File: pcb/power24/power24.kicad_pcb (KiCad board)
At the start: 2 copper layers, 47.8 x 64 mm, 24 parts, among them P1 CONN_3X2, P2 CONN_4X2, P3 CONN_2, U1 MC34063

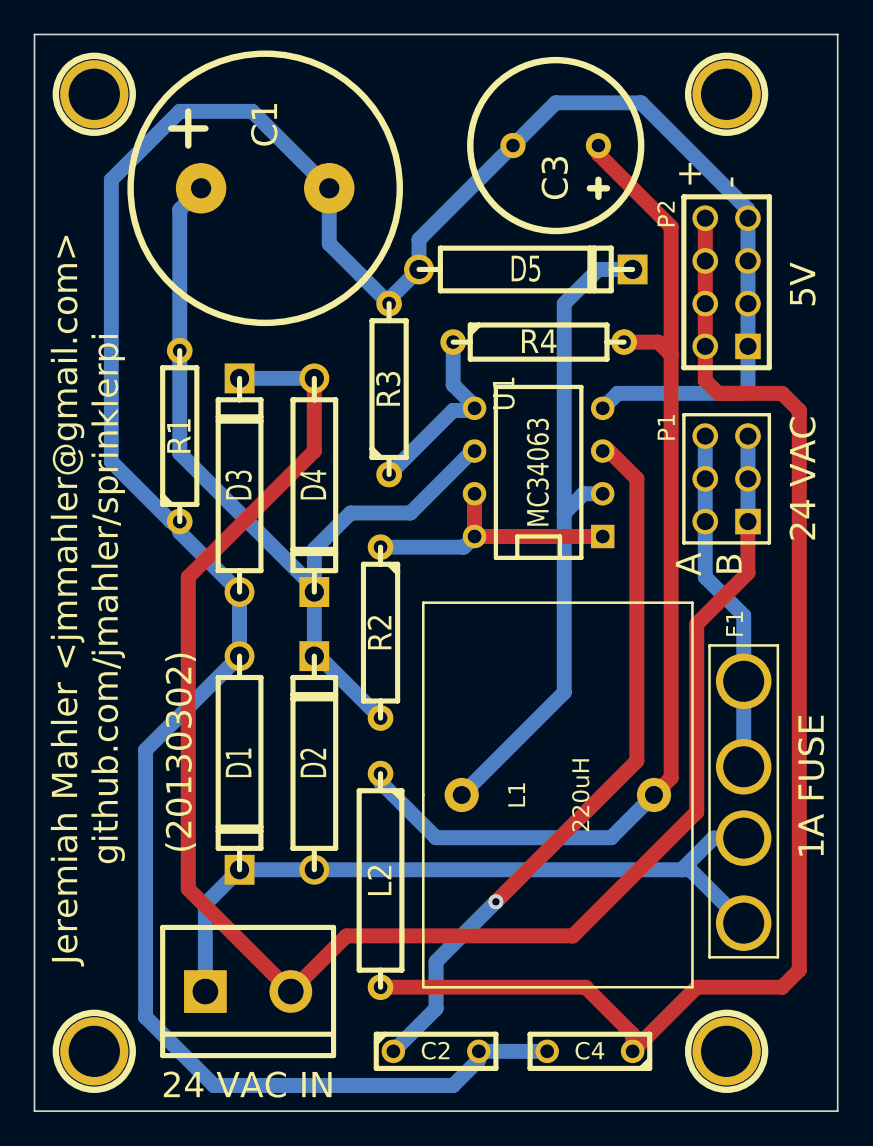
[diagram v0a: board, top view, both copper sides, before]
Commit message: general cleanup of power24 PCB
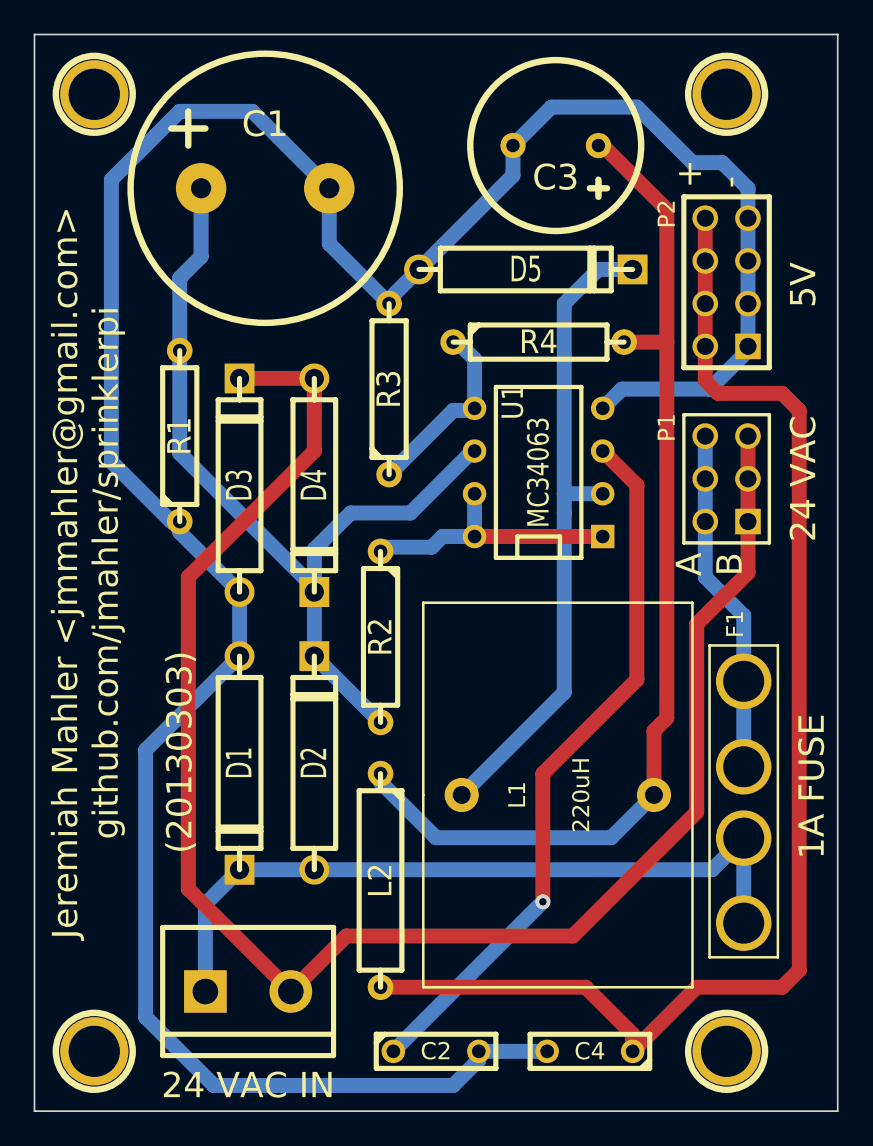
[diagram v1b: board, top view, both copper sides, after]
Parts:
- moved R2 0.25 mm to (165.9, 87.1)
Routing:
- net GND: track 157.0 -> 156.2 mm
- net N-0000012: track 63.1 -> 62.5 mm
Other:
- board text added: "(20130303)"
- board text removed: "(20130302)"

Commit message: added power LED to power24 circuit
An LED has been added that lights when power is applied (power24).
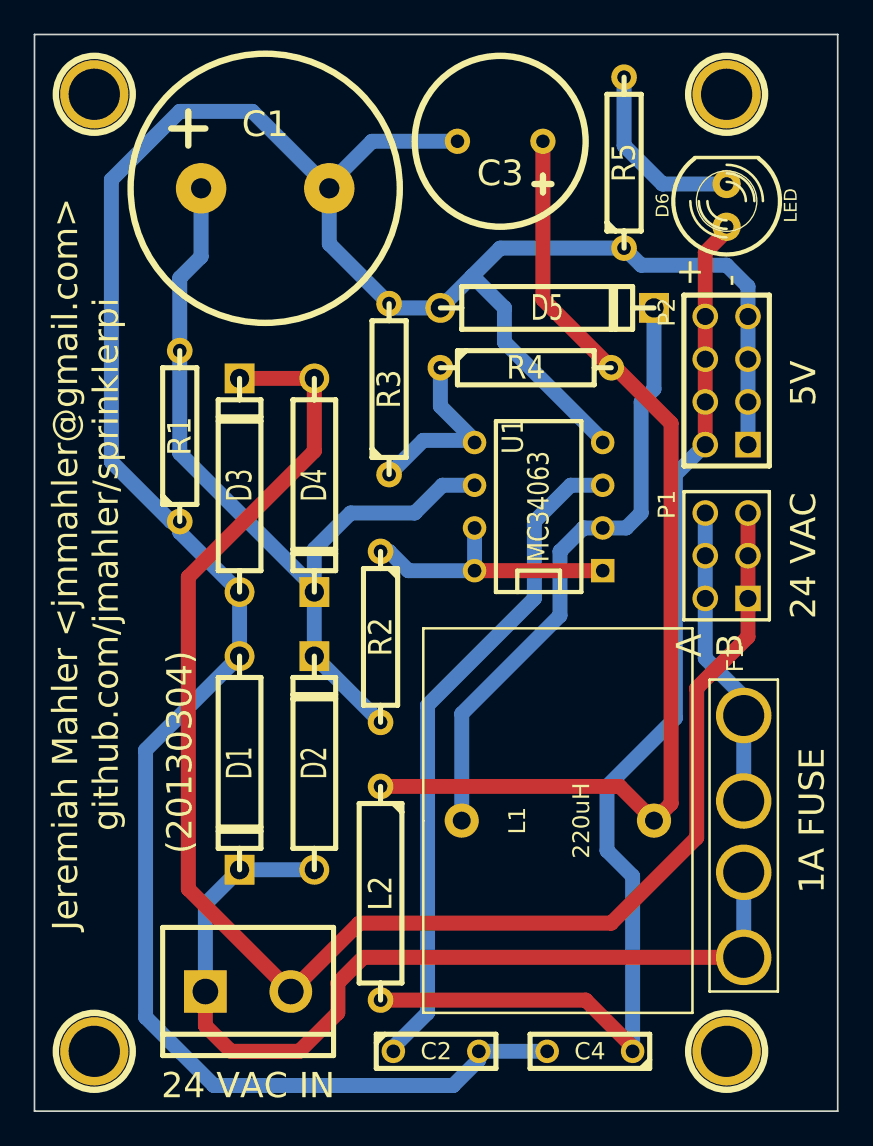
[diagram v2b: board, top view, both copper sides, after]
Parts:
- added D6: LED, LED-5MM, F.Cu at (186.4, 61.5)
- added R5: 330, R4, F.Cu at (180.3, 58.9)
- moved P2 5.84 mm to (186.4, 71.9)
- moved P1 4.57 mm to (186.4, 82.3)
- moved C3 3.31 mm to (173.0, 57.7)
- moved D5 2.62 mm to (175.8, 67.6)
- moved F1 2.03 mm to (187.5, 98.6)
- moved U1 2.03 mm to (175.3, 79.4)
- moved R4 1.70 mm to (174.5, 71.1)
- moved L1 1.52 mm to (176.3, 98.0)
- moved L2 0.76 mm to (165.9, 102.4)
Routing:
- net N-000005: track 43.9 -> 55.6 mm
- net N-000003: track 0.00 -> 11.1 mm
- net N-000004: track 78.3 -> 69.0 mm
- net GND: track 156.2 -> 162.4 mm
- net N-000007: track 98.7 -> 95.0 mm
- net N-0000010: track 42.5 -> 39.9 mm, vias 1 -> 0
- net N-000001: track 20.6 -> 18.1 mm
- net N-0000012: track 38.9 -> 36.7 mm
- net N-0000013: track 62.5 -> 61.2 mm
- net N-000008: track 51.7 -> 50.9 mm
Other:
- net class Default: clearance 0.254 -> 0.381
- rule trace_clearance: 0.254 -> 0.381
- board text added: "(20130304)"
- board text removed: "(20130303)"

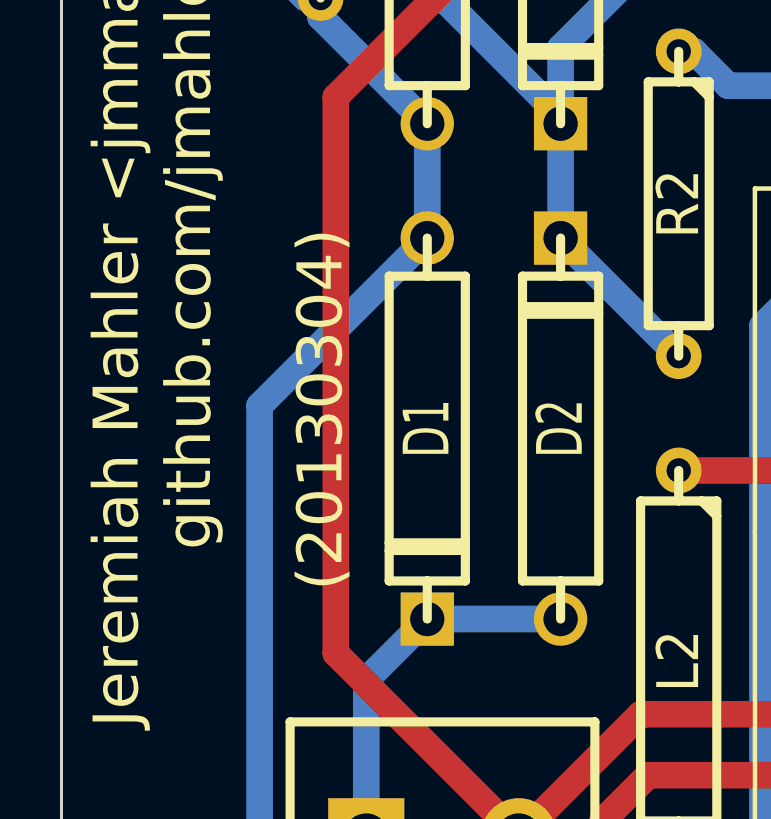
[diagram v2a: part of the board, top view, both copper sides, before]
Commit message: fixed power24 PCB date
The date on the PCB silkscreen for the power24 PCB
was wrong.  Fixed.
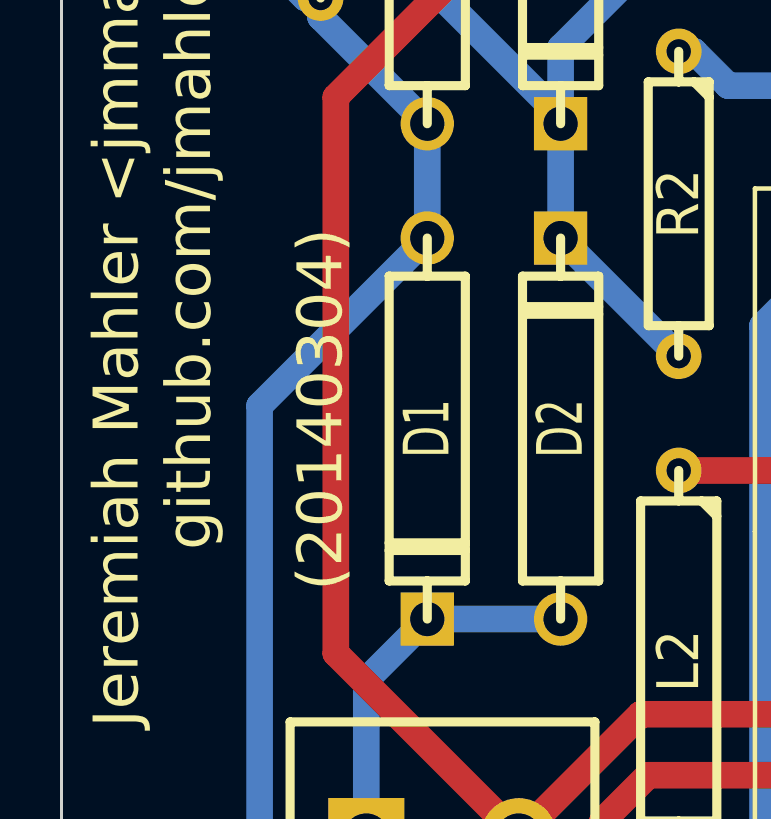
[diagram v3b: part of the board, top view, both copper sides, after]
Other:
- board text added: "(20140304)"
- board text removed: "(20130304)"
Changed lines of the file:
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@@
   )
   (setup
-    (last_trace_width 0.889)
+    (last_trace_width 0.254)
     (user_trace_width 0.254)
     (user_trace_width 0.3048)
@@
   (gr_line (start 193.04 51.308) (end 193.04 115.316) (angle 90) (layer Edge.Cuts) (width 0.1))
   (gr_line (start 145.288 51.308) (end 193.04 51.308) (angle 90) (layer Edge.Cuts) (width 0.1))
-  (gr_text "(20130304)" (at 153.924 93.98 90) (layer F.SilkS)
+  (gr_text "(20140304)" (at 153.924 93.98 90) (layer F.SilkS)
     (effects (font (size 1.5 1.5) (thickness 0.3)))
   )

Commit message: updated power24 for 3.3v operation
Updated the schematic of the power supply module
(power24) for 3.3v operation instead of 5v.
The only change was the voltage divider resistors
to the MC34063.  Note, the PCB label has not
been changed from 5V to 3.3V.  This can be done
in the next PCB revision.
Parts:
- R3: value 2.2k -> 3k
- R4: value 6.6k -> 5k
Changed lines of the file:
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@@
       (effects (font (size 1.397 1.27) (thickness 0.2032)))
     )
-    (fp_text value 2.2k (at 0 0 90) (layer F.SilkS) hide
+    (fp_text value 3k (at 0 0 90) (layer F.SilkS) hide
       (effects (font (size 1.397 1.27) (thickness 0.2032)))
     )
@@
       (effects (font (size 1.397 1.27) (thickness 0.2032)))
     )
-    (fp_text value 6.6k (at 0 0) (layer F.SilkS) hide
+    (fp_text value 5k (at 0 0) (layer F.SilkS) hide
       (effects (font (size 1.397 1.27) (thickness 0.2032)))
     )
